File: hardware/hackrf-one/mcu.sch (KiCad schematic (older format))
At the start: 134 parts, among them J1 USB-MICRO-B, P1 1V8, P20 GPIO, P22 I2S, P23 DBGEN, P24 TRST, P25 LPC_ISP, P26 LPC_JTAG, P28 SD, P29 CPLD_JTAG, P3 GND, P30 BANK2_AUX, P5 LEDS, P68 SPIFI_CS, P69 VREGMODE, P70 EN_1V8, P71 ID, P72 GP_CLKIN, P73 P1_2, P74 P1_1, P75 GP_CLKIN, P76 GP_CLKIN, P77 GP_CLKIN, P78 GP_CLKIN, P79 GP_CLKIN, P8 VCC, P80 SHIELD, P81 SPIFI_SIO2, P82 SPIFI_SIO3, Q5 MOSFET_P, SW1 DFU, SW2 RESET, U15 TVS, U20 W25Q80, U21 TPS62410, U23 LPC4320FBD144, U24 GSG-XC2C64A-7VQG100C, X2 MCU_XTAL, X3 RTC_XTAL

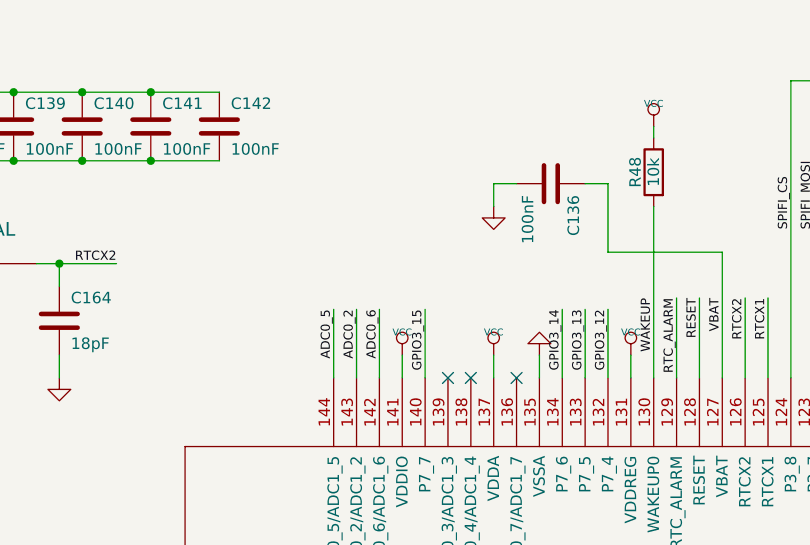
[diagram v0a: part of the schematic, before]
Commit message: HackRF One: added ADC pin straps for hardware version detection
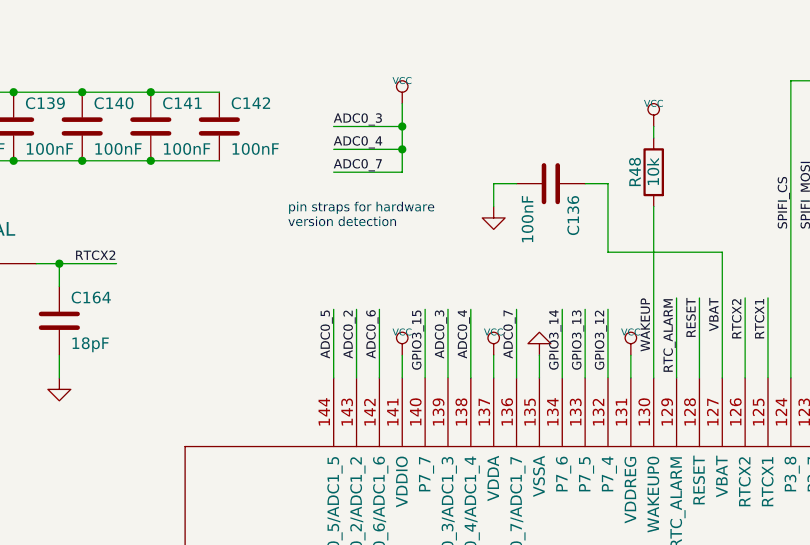
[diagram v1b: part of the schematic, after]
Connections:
- net VCC: now also U23.136 (ADC0_7/ADC1_7), U23.138 (ADC0_4/ADC1_4), U23.139 (ADC0_3/ADC1_3)
- no-connect marks 17 -> 14
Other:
- note added: "pin straps for hardware\nversion detection"
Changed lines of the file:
@@
 Text Label 10700 4200 2    40   ~ 0
 ISP
-NoConn ~ 5750 2050
-NoConn ~ 5850 2050
-NoConn ~ 6050 2050
 $Comp
 L VCC #PWR0262
@@
 	-1   0    0    1
 $EndComp
+$Comp
+L VCC #PWR?
+U 1 1 5BF1000A
+P 5550 850
+F 0 "#PWR?" H 5550 950 30  0001 C CNN
+F 1 "VCC" H 5550 950 30  0000 C CNN
+F 2 "" H 5550 850 60  0001 C CNN
+F 3 "" H 5550 850 60  0001 C CNN
+	1    5550 850
+	1    0    0    -1
+$EndComp
+Text Label 5750 1750 3    40   ~ 0
+ADC0_3
+Text Label 5850 1750 3    40   ~ 0
+ADC0_4
+Text Label 6050 1750 3    40   ~ 0
+ADC0_7
+Text Label 5250 950  0    40   ~ 0
+ADC0_3
+Text Label 5250 1050 0    40   ~ 0
+ADC0_4
+Text Label 5250 1150 0    40   ~ 0
+ADC0_7
+Wire Wire Line
+	5250 950  5550 950
+Wire Wire Line
+	5550 850  5550 1150
+Wire Wire Line
+	5550 1050 5250 1050
+Connection ~ 5550 950
+Wire Wire Line
+	5550 1150 5250 1150
+Connection ~ 5550 1050
+Wire Wire Line
+	6050 1750 6050 2050
+Wire Wire Line
+	5850 1750 5850 2050
+Wire Wire Line
+	5750 2050 5750 1750
+Text Notes 5050 1400 0    40   ~ 0
+pin straps for hardware\nversion detection
 $EndSCHEMATC

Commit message: HackRF One: replaced R69 for part availability
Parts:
- R69: Manufacturer Rohm -> Yageo; Part Number MCR01MRTF1202 -> RC0402FR-0712KL
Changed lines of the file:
@@
 F 2 "hackrf:GSG-0402" H 3850 5300 60  0001 C CNN
 F 3 "" H 3850 5300 60  0001 C CNN
-F 4 "Rohm" H 3850 5300 60  0001 C CNN "Manufacturer"
-F 5 "MCR01MRTF1202" H 3850 5300 60  0001 C CNN "Part Number"
+F 4 "Yageo" H 3850 5300 60  0001 C CNN "Manufacturer"
+F 5 "RC0402FR-0712KL" H 3850 5300 60  0001 C CNN "Part Number"
 F 6 "RES 12.0K OHM 1/16W 1% 0402 SMD" H 3850 5300 60  0001 C CNN "Description"
 	1    3850 5300

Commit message: HackRF One: replaced various capacitors that are NRND
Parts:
- C118, C157, C158, C164: Manufacturer Murata -> Samsung; Part Number GRM1555C1H180JA01D -> CL05C180JB5NNN
- C156: Part Number GRM1555C1H470JA01D -> GCM1555C1H470JA16
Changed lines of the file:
@@
 F 2 "hackrf:GSG-0402" H 5000 9900 60  0001 C CNN
 F 3 "" H 5000 9900 60  0001 C CNN
-F 4 "Murata" H 5000 9900 60  0001 C CNN "Manufacturer"
-F 5 "GRM1555C1H180JA01D" H 5000 9900 60  0001 C CNN "Part Number"
+F 4 "Samsung" H 5000 9900 60  0001 C CNN "Manufacturer"
+F 5 "CL05C180JB5NNN" H 5000 9900 60  0001 C CNN "Part Number"
 F 6 "CAP CER 18PF 50V 5% NP0 0402" H 5000 9900 60  0001 C CNN "Description"
 	1    5000 9900
@@
 F 3 "" H 5550 9900 60  0001 C CNN
 F 4 "Murata" H 7150 11000 60  0001 C CNN "Manufacturer"
-F 5 "GRM1555C1H470JA01D" H 7150 11000 60  0001 C CNN "Part Number"
+F 5 "GCM1555C1H470JA16" H 7150 11000 60  0001 C CNN "Part Number"
 F 6 "CAP CER 47PF 50V 5% NP0 0402" H 7150 11000 60  0001 C CNN "Description"
 F 7 "DNP" V 5850 9900 60  0000 C CNN "Note"
@@
 F 2 "hackrf:GSG-0402" H 4200 9900 60  0001 C CNN
 F 3 "" H 4200 9900 60  0001 C CNN
-F 4 "Murata" H 4200 9900 60  0001 C CNN "Manufacturer"
-F 5 "GRM1555C1H180JA01D" H 4200 9900 60  0001 C CNN "Part Number"
+F 4 "Samsung" H 4200 9900 60  0001 C CNN "Manufacturer"
+F 5 "CL05C180JB5NNN" H 4200 9900 60  0001 C CNN "Part Number"
 F 6 "CAP CER 18PF 50V 5% NP0 0402" H 4200 9900 60  0001 C CNN "Description"
 	1    4200 9900
@@
 F 2 "hackrf:GSG-0402" H 4050 1800 60  0001 C CNN
 F 3 "" H 4050 1800 60  0001 C CNN
-F 4 "Murata" H 4050 1800 60  0001 C CNN "Manufacturer"
-F 5 "GRM1555C1H180JA01D" H 4050 1800 60  0001 C CNN "Part Number"
+F 4 "Samsung" H 4050 1800 60  0001 C CNN "Manufacturer"
+F 5 "CL05C180JB5NNN" H 4050 1800 60  0001 C CNN "Part Number"
 F 6 "CAP CER 18PF 50V 5% NP0 0402" H 4050 1800 60  0001 C CNN "Description"
 	1    4050 1800
@@
 F 2 "hackrf:GSG-0402" H 3250 1800 60  0001 C CNN
 F 3 "" H 3250 1800 60  0001 C CNN
-F 4 "Murata" H 3250 1800 60  0001 C CNN "Manufacturer"
-F 5 "GRM1555C1H180JA01D" H 3250 1800 60  0001 C CNN "Part Number"
+F 4 "Samsung" H 3250 1800 60  0001 C CNN "Manufacturer"
+F 5 "CL05C180JB5NNN" H 3250 1800 60  0001 C CNN "Part Number"
 F 6 "CAP CER 18PF 50V 5% NP0 0402" H 3250 1800 60  0001 C CNN "Description"
 	1    3250 1800

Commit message: HackRF One: corrected R65 part selection
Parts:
- R65: Description RES SMD 18K OHM 5% 1/10W 0603 -> RES SMD 18K OHM 5% 1/16W 0402; Part Number RC0603JR-0718KL -> RC0402JR-0718KL
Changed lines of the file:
@@
 F 3 "" H 2900 4700 60  0001 C CNN
 F 4 "Yageo" H 2900 4700 60  0001 C CNN "Manufacturer"
-F 5 "RC0603JR-0718KL" H 2900 4700 60  0001 C CNN "Part Number"
-F 6 "RES SMD 18K OHM 5% 1/10W 0603" H 2900 4700 60  0001 C CNN "Description"
+F 5 "RC0402JR-0718KL" H 2900 4700 60  0001 C CNN "Part Number"
+F 6 "RES SMD 18K OHM 5% 1/16W 0402" H 2900 4700 60  0001 C CNN "Description"
 	1    2900 4700
 	-1   0    0    1
